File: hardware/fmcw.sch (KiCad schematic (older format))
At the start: 20 parts, among them P5 CONN_01X01, P7 CONN_01X01, P8 CONN_01X01, U2 LP5907-1.8, U4 KT2520K, U5 NC7S04P5X, U6 NB3N551

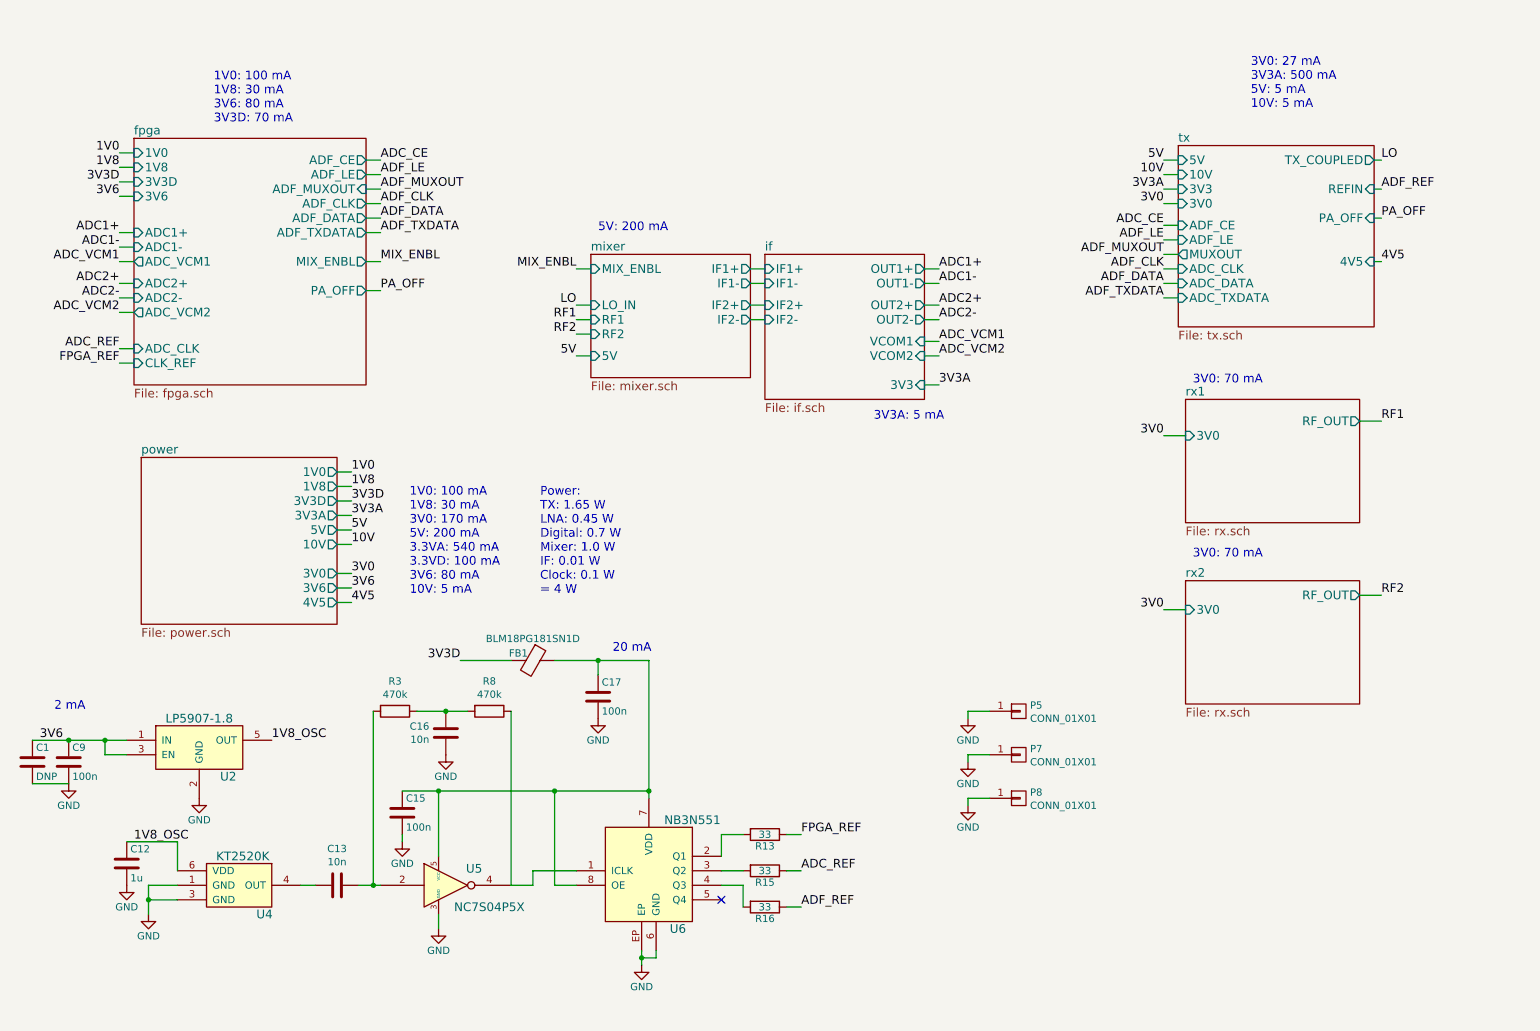
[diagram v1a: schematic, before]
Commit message: Adjusted power supply for new power amplifier.
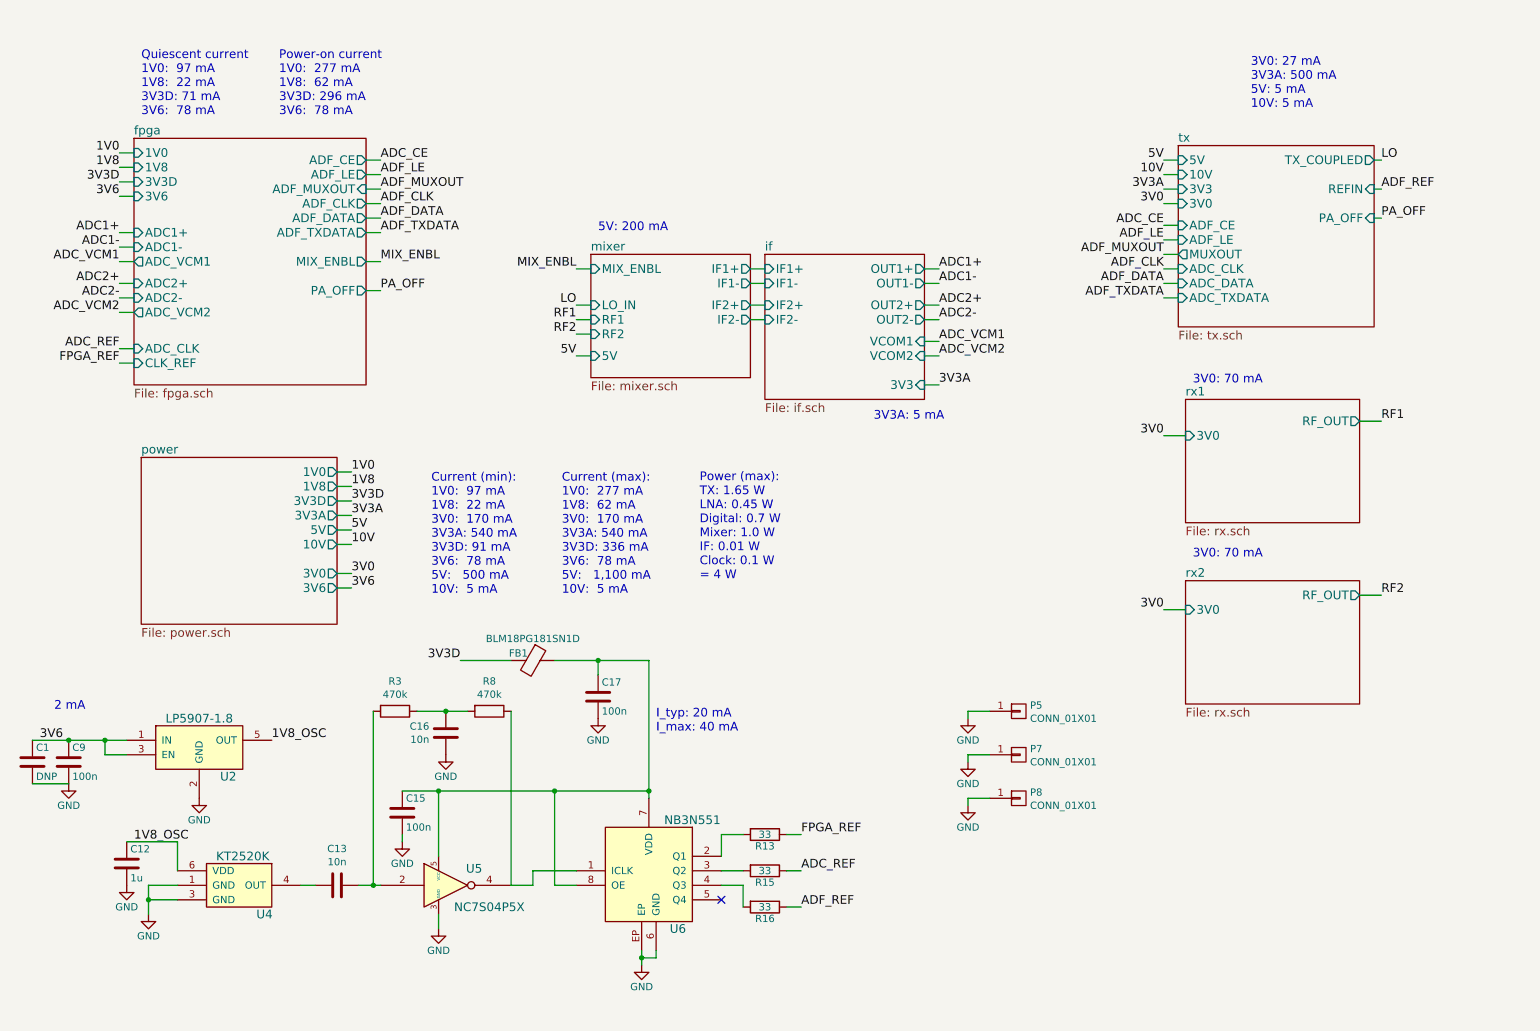
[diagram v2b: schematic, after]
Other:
- note added: "Current (max):\n1V0: 277 mA\n1V8: 62 mA\n3V0: 170 mA\n3V3A: 540 mA\n3V3D: 336 mA\n3V6: 78 mA\n5V: 1,100 mA\n10V: 5 mA"
- note added: "Current (min):\n1V0: 97 mA\n1V8: 22 mA\n3V0: 170 mA\n3V3A: 540 mA\n3V3D: 91 mA\n3V6: 78 mA\n5V: 500 mA\n10V: 5 mA"
- note added: "I_typ: 20 mA\nI_max: 40 mA"
- note added: "Power (max):\nTX: 1.65 W\nLNA: 0.45 W\nDigital: 0.7 W\nMixer: 1.0 W\nIF: 0.01 W\nClock: 0.1 W\n= 4 W"
- note added: "Power-on current\n1V0: 277 mA\n1V8: 62 mA\n3V3D: 296 mA\n3V6: 78 mA"
- note added: "Quiescent current\n1V0: 97 mA\n1V8: 22 mA\n3V3D: 71 mA\n3V6: 78 mA"
- note removed: "1V0: 100 mA\n1V8: 30 mA\n3V0: 170 mA\n5V: 200 mA\n3.3VA: 540 mA\n3.3VD: 100 mA\n3V6: 80 mA\n10V: 5 mA"
- note removed: "1V0: 100 mA\n1V8: 30 mA\n3V6: 80 mA\n3V3D: 70 mA"
- note removed: "20 mA"
- note removed: "Power:\nTX: 1.65 W\nLNA: 0.45 W\nDigital: 0.7 W\nMixer: 1.0 W\nIF: 0.01 W\nClock: 0.1 W\n= 4 W"
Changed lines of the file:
@@
 EESchema Schematic File Version 4
 LIBS:fmcw-cache
-EELAYER 29 0
+EELAYER 26 0
 EELAYER END
 $Descr A4 11693 8268
@@
 F13 "3V0" I L 8800 2150 60
 F14 "PA_OFF" I R 10150 2250 60
-F15 "4V5" I R 10150 2550 60
 $EndSheet
 $Sheet
@@
 F8 "3V6" O R 3000 4800 60
 F9 "10V" O R 3000 4500 60
-F10 "4V5" O R 3000 4900 60
 $EndSheet
 $Sheet
@@
 	1    0    0    -1
 $EndComp
-Text Notes 3500 4850 0    60   ~ 0
-1V0: 100 mA\n1V8: 30 mA\n3V0: 170 mA\n5V: 200 mA\n3.3VA: 540 mA\n3.3VD: 100 mA\n3V6: 80 mA\n10V: 5 mA
+Text Notes 4550 4850 0    60   ~ 0
+Current (max):\n1V0:  277 mA\n1V8:  62 mA\n3V0:  170 mA\n3V3A: 540 mA\n3V3D: 336 mA\n3V6:  78 mA\n5V:   1,100 mA\n10V:  5 mA
 Text Notes 9300 1500 0    60   ~ 0
 3V0: 27 mA\n3V3A: 500 mA\n5V: 5 mA\n10V: 5 mA
 Text Notes 6700 3650 0    60   ~ 0
 3V3A: 5 mA
-Text Notes 2150 1600 0    60   ~ 0
-1V0: 100 mA\n1V8: 30 mA\n3V6: 80 mA\n3V3D: 70 mA
-Text Notes 4900 5250 0    60   ~ 0
-20 mA
-Text Notes 4400 4850 0    60   ~ 0
-Power:\nTX: 1.65 W\nLNA: 0.45 W\nDigital: 0.7 W\nMixer: 1.0 W\nIF: 0.01 W\nClock: 0.1 W\n= 4 W
+Text Notes 5200 5800 0    60   ~ 0
+I_typ: 20 mA\nI_max: 40 mA
+Text Notes 5500 4750 0    60   ~ 0
+Power (max):\nTX: 1.65 W\nLNA: 0.45 W\nDigital: 0.7 W\nMixer: 1.0 W\nIF: 0.01 W\nClock: 0.1 W\n= 4 W
 Text Notes 8900 3400 0    60   ~ 0
 3V0: 70 mA
@@
 	5800 6850 5800 7000
 Wire Wire Line
-	10150 2550 10200 2550
-Text Label 10200 2550 0    60   ~ 0
-4V5
-Wire Wire Line
-	3000 4900 3100 4900
-Text Label 3100 4900 0    60   ~ 0
-4V5
-Wire Wire Line
 	4500 5300 4800 5300
 Wire Wire Line
@@
 Wire Wire Line
 	3450 6500 3450 6550
+Text Notes 1650 1550 0    60   ~ 0
+Quiescent current\n1V0:  97 mA\n1V8:  22 mA\n3V3D: 71 mA\n3V6:  78 mA
+Text Notes 2600 1550 0    60   ~ 0
+Power-on current\n1V0:  277 mA\n1V8:  62 mA\n3V3D: 296 mA\n3V6:  78 mA
+Text Notes 3650 4850 0    60   ~ 0
+Current (min):\n1V0:  97 mA\n1V8:  22 mA\n3V0:  170 mA\n3V3A: 540 mA\n3V3D: 91 mA\n3V6:  78 mA\n5V:   500 mA\n10V:  5 mA
 $EndSCHEMATC

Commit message: Documentation for TPS5420D buck converter.
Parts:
- FB1: MFN (none) -> BLM18PG181SH1D; manf# BLM18PG181SH1D -> (none)
- U2: MFN (none) -> LP5907MFX-1.8/NOPB; manf# LP5907MFX-1.8/NOPB -> (none)
- U4: MFN (none) -> KT2520K40000DAW18TAS; manf# KT2520K40000DAW18TAS -> (none)
- U5: MFN (none) -> NC7S04P5X; manf# NC7S04P5X -> (none)
- U6: MFN (none) -> NB3N551MNR4G; manf# NB3N551MNR4G -> (none)
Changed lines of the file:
@@
 F 2 "fmcw:KT2520K" H 2300 6800 60  0001 C CNN
 F 3 "https://media.digikey.com/pdf/Data%20Sheets/AVX%20PDFs/KT2520K40000DAW18TAS_Spec.pdf" H 2300 6800 60  0001 C CNN
-F 4 "KT2520K40000DAW18TAS" H 2300 6800 50  0001 C CNN "manf#"
+F 4 "" H 2300 6800 50  0001 C CNN "manf#"
+F 5 "KT2520K40000DAW18TAS" H 0   0   50  0001 C CNN "MFN"
 	1    2300 6800
 	1    0    0    -1
@@
 F 2 "Package_TO_SOT_SMD:SOT-353_SC-70-5" H 3750 6850 60  0001 C CNN
 F 3 "https://www.fairchildsemi.com/datasheets/NC/NC7S04.pdf" H 3750 6850 60  0001 C CNN
-F 4 "NC7S04P5X" H 3750 6850 50  0001 C CNN "manf#"
+F 4 "" H 3750 6850 50  0001 C CNN "manf#"
+F 5 "NC7S04P5X" H 0   0   50  0001 C CNN "MFN"
 	1    3750 6850
 	1    0    0    -1
@@
 F 2 "fmcw:DFN-8" H 5150 6800 60  0001 C CNN
 F 3 "http://www.onsemi.com/pub/Collateral/NB3N551-D.PDF" H 5150 6800 60  0001 C CNN
-F 4 "NB3N551MNR4G" H 5150 6800 50  0001 C CNN "manf#"
+F 4 "" H 5150 6800 50  0001 C CNN "manf#"
+F 5 "NB3N551MNR4G" H 0   0   50  0001 C CNN "MFN"
 	1    5150 6800
 	1    0    0    -1
@@
 F 2 "fmcw:C_0603b" H 4350 5300 60  0001 C CNN
 F 3 "https://www.murata.com/en-us/products/productdata/8796738650142/ENFA0003.pdf" H 4350 5300 60  0001 C CNN
-F 4 "BLM18PG181SH1D" H 4350 5300 50  0001 C CNN "manf#"
+F 4 "" H 4350 5300 50  0001 C CNN "manf#"
+F 5 "BLM18PG181SH1D" H 0   0   50  0001 C CNN "MFN"
 	1    4350 5300
 	0    1    1    0
@@
 F 2 "fmcw:SOT-23-5" H 2050 5950 60  0001 C CNN
 F 3 "http://www.ti.com/lit/ds/symlink/lp5907.pdf" H 2050 5950 60  0001 C CNN
-F 4 "LP5907MFX-1.8/NOPB" H 2050 5900 50  0001 C CNN "manf#"
+F 4 "" H 2050 5900 50  0001 C CNN "manf#"
+F 5 "LP5907MFX-1.8/NOPB" H 0   0   50  0001 C CNN "MFN"
 	1    2050 5900
 	1    0    0    -1

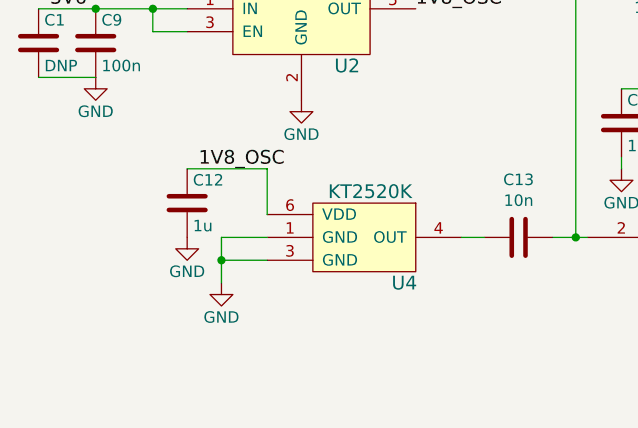
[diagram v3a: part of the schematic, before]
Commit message: Improved top level documentation.
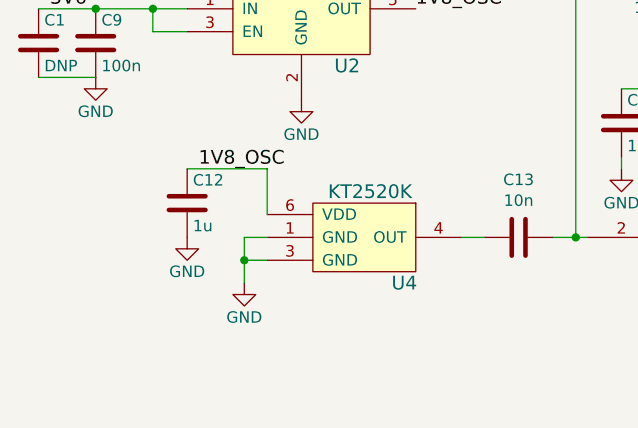
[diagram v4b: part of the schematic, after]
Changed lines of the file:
@@
 F 2 "fmcw:KT2520K" H 2300 6800 60  0001 C CNN
 F 3 "https://media.digikey.com/pdf/Data%20Sheets/AVX%20PDFs/KT2520K40000DAW18TAS_Spec.pdf" H 2300 6800 60  0001 C CNN
-F 4 "" H 2300 6800 50  0001 C CNN "manf#"
-F 5 "KT2520K40000DAW18TAS" H 0   0   50  0001 C CNN "MFN"
+F 4 "KT2520K40000DAW18TAS" H 0   0   50  0001 C CNN "MFN"
 	1    2300 6800
 	1    0    0    -1
@@
 L power:GND #PWR01
 U 1 1 597314F3
-P 1700 7050
-F 0 "#PWR01" H 1700 6800 50  0001 C CNN
-F 1 "GND" H 1700 6900 50  0000 C CNN
-F 2 "" H 1700 7050 60  0000 C CNN
-F 3 "" H 1700 7050 60  0000 C CNN
-	1    1700 7050
+P 1800 7050
+F 0 "#PWR01" H 1800 6800 50  0001 C CNN
+F 1 "GND" H 1800 6900 50  0000 C CNN
+F 2 "" H 1800 7050 60  0000 C CNN
+F 3 "" H 1800 7050 60  0000 C CNN
+	1    1800 7050
 	1    0    0    -1
 $EndComp
@@
 	8700 2800 8800 2800
 Wire Wire Line
-	1900 6950 1700 6950
-Wire Wire Line
-	1700 6850 1700 6950
-Wire Wire Line
-	1900 6850 1700 6850
-Connection ~ 1700 6950
+	1800 6850 1800 6950
+Connection ~ 1800 6950
 Wire Wire Line
 	1900 6550 1900 6750
@@
 3V0: 70 mA
 Wire Wire Line
-	1700 6950 1700 7050
+	1800 6950 1800 7050
 Wire Wire Line
 	1400 5850 1550 5850
@@
 Text Notes 3650 4850 0    60   ~ 0
 Current (min):\n1V0:  97 mA\n1V8:  22 mA\n3V0:  170 mA\n3V3A: 540 mA\n3V3D: 91 mA\n3V6:  78 mA\n5V:   500 mA\n10V:  5 mA
+Wire Wire Line
+	1900 6850 1800 6850
+Wire Wire Line
+	1900 6950 1800 6950
 $EndSCHEMATC

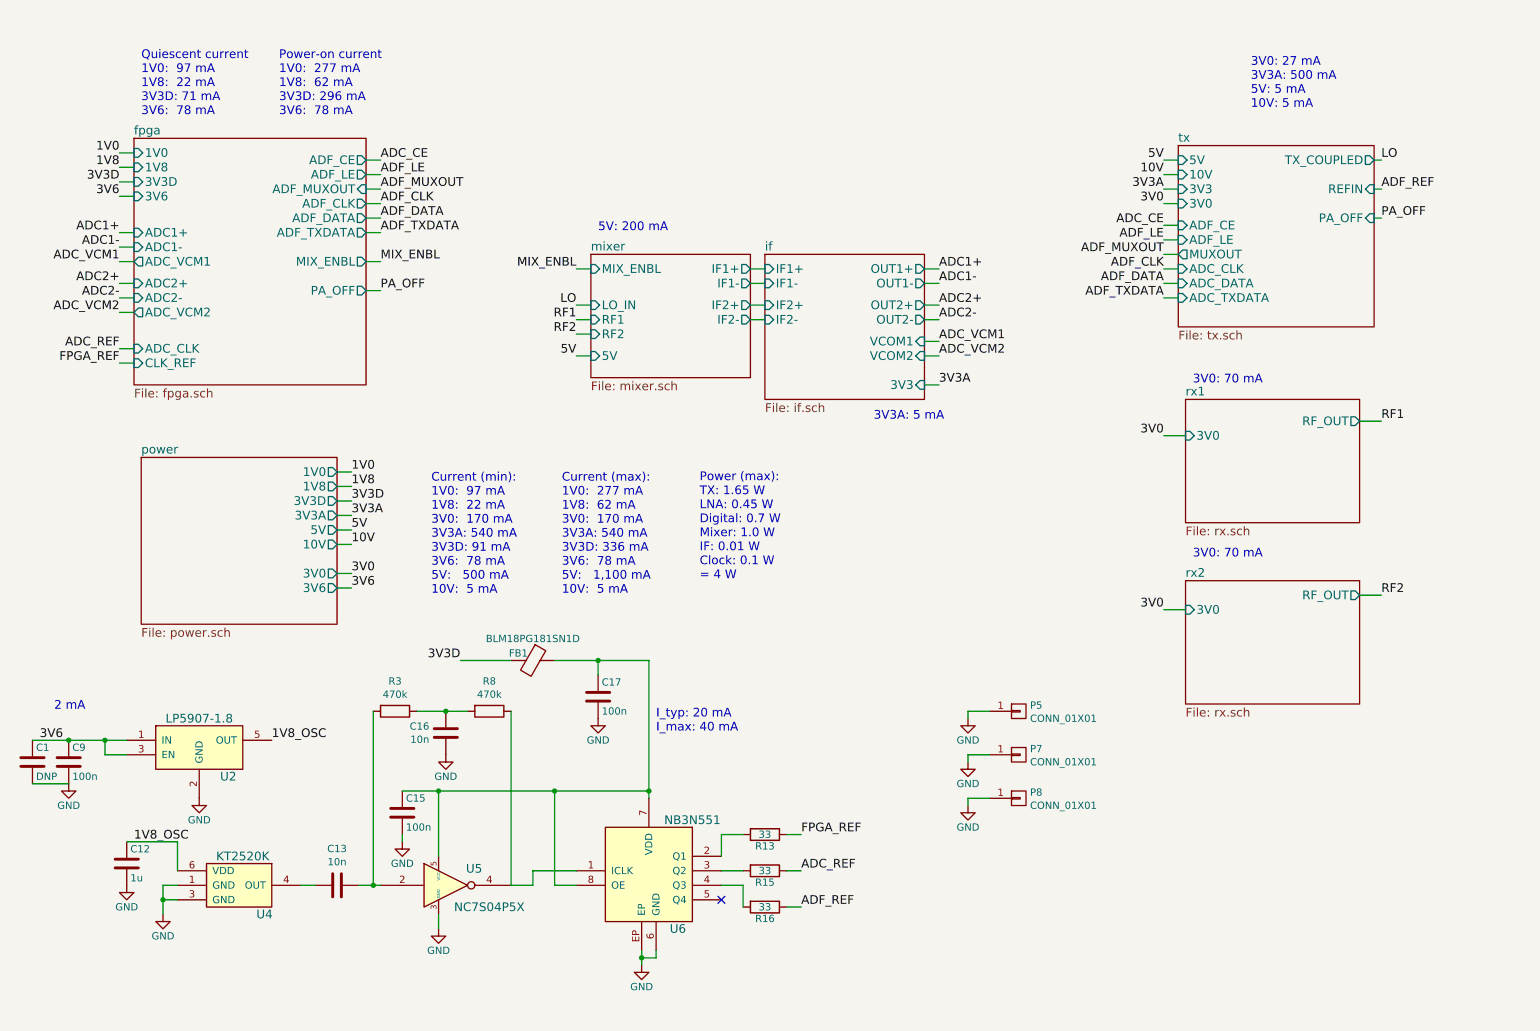
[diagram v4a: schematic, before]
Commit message: Added MFNs to components.
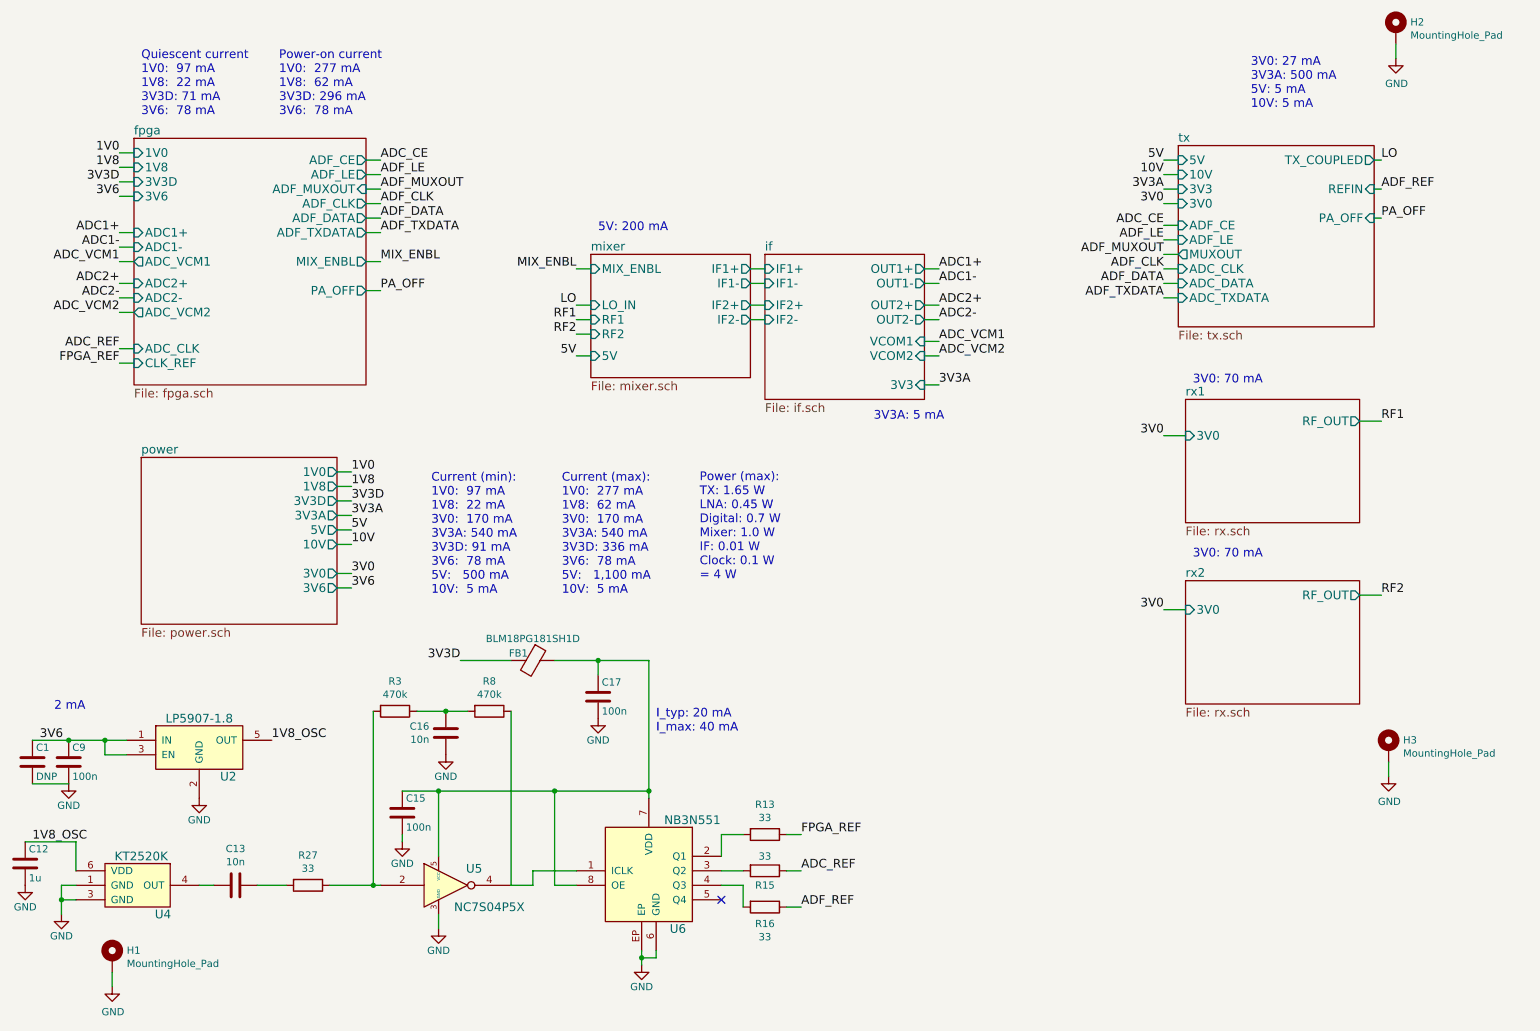
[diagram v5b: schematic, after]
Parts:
- removed P5, P7, P8: CONN_01X01, fmcw:MountingHole_3.2mm_M3_Pad_Via_mod, symbol fmcw-rescue:CONN_01X01-fmcw3-rescue
- added H1, H2, H3: MountingHole_Pad, MountingHole:MountingHole_3.2mm_M3_Pad_Via, symbol Mechanical:MountingHole_Pad
- added R27: 33, Resistor_SMD:R_0402_1005Metric, symbol Device:R
- C12: MFN (none) -> CL10B105MO8NNWC
- C13, C16: MFN (none) -> GRM155R71E103KA01D
- C15, C17, C9: MFN (none) -> CL05B104KO5NNNC
- FB1: value BLM18PG181SN1D -> BLM18PG181SH1D; footprint fmcw:C_0603b -> Inductor_SMD:L_0603_1608Metric
- R13, R15, R16: footprint fmcw:R_0402b -> Resistor_SMD:R_0402_1005Metric; MFN (none) -> ERJ-2GEJ330X
- R3, R8: footprint fmcw:R_0402b -> Resistor_SMD:R_0402_1005Metric; MFN (none) -> ERJ-2RKF4702X
- U2: footprint fmcw:SOT-23-5 -> Package_TO_SOT_SMD:SOT-23-5
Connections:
- net GND: now also H1.1, H2.1, H3.1
- net at R3.2, U5.2: now also R27.1; no longer C13.1
- new net: C13.1, R27.2
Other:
- moved on the sheet: C12, C13, U4
